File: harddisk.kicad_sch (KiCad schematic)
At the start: 12 parts, among them IC45 74HCT573, IC46 74HCT573, J1 IDC 44-pin IDE

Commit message: fix 44-pin ide
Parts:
- J1: footprint Connector_IDC:IDC-Header_2x22_P2.54mm_Vertical -> Connector_PinHeader_2.00mm:PinHeader_2x22_P2.00mm_Vertical
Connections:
- no-connect marks 6 -> 7
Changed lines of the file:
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@@
 	)
 	(no_connect
+		(at 74.93 66.04)
+	)
+	(no_connect
 		(at 74.93 60.96)
 	)
@@
 			)
 		)
-		(property "Footprint" "Connector_IDC:IDC-Header_2x22_P2.54mm_Vertical"
+		(property "Footprint" "Connector_PinHeader_2.00mm:PinHeader_2x22_P2.00mm_Vertical"
 			(at 80.01 53.34 0)
 			(effects

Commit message: prepare for fabrication
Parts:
- C217: LCSC (none) -> C344201; LCSC Part (none) -> C344201
- C75, C97: LCSC (none) -> C49678; LCSC Part (none) -> C49678
- IC45, IC46: LCSC (none) -> C52145555; LCSC Part (none) -> C52145555
- R204: LCSC (none) -> C2907326; LCSC Part (none) -> C2907326
- R205: LCSC (none) -> C2907219; LCSC Part (none) -> C2907219
- R206: LCSC (none) -> C2933293; LCSC Part (none) -> C2933293
- RN1: value 68R -> 68Rx8; LCSC (none) -> C1739978; LCSC Part (none) -> C1739978
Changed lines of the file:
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@@
+			)
+		)
+		(property "LCSC" "C2907326"
+			(at 97.79 81.28 90)
+			(effects
+				(font
+					(size 1.27 1.27)
+				)
+				(hide yes)
+			)
+		)
+		(property "LCSC Part" "C2907326"
+			(at 97.79 81.28 90)
+			(effects
+				(font
+					(size 1.27 1.27)
+				)
+				(hide yes)
 			)
 		)
@@
 		(property "Description" "Resistor, small symbol"
 			(at 115.57 63.5 0)
+			(effects
+				(font
+					(size 1.27 1.27)
+				)
+				(hide yes)
+			)
+		)
+		(property "LCSC" "C2907219"
+			(at 115.57 63.5 90)
+			(effects
+				(font
+					(size 1.27 1.27)
+				)
+				(hide yes)
+			)
+		)
+		(property "LCSC Part" "C2907219"
+			(at 115.57 63.5 90)
 			(effects
 				(font
@@
 			)
 		)
+		(property "LCSC" "C52145555"
+			(at 140.97 111.76 0)
+			(effects
+				(font
+					(size 1.27 1.27)
+				)
+				(hide yes)
+			)
+		)
+		(property "LCSC Part" "C52145555"
+			(at 140.97 111.76 0)
+			(effects
+				(font
+					(size 1.27 1.27)
+				)
+				(hide yes)
+			)
+		)
 		(pin "3"
 		)
@@
 		(property "Description" "Unpolarized capacitor, small symbol"
 			(at 62.23 161.29 0)
+			(effects
+				(font
+					(size 1.27 1.27)
+				)
+				(hide yes)
+			)
+		)
+		(property "LCSC" "C49678"
+			(at 62.23 161.29 90)
+			(effects
+				(font
+					(size 1.27 1.27)
+				)
+				(hide yes)
+			)
+		)
+		(property "LCSC Part" "C49678"
+			(at 62.23 161.29 90)
 			(effects
 				(font
@@
 			)
 		)
+		(property "LCSC" "C344201"
+			(at 128.27 38.1 0)
+			(effects
+				(font
+					(size 1.27 1.27)
+				)
+				(hide yes)
+			)
+		)
+		(property "LCSC Part" "C344201"
+			(at 128.27 38.1 0)
+			(effects
+				(font
+					(size 1.27 1.27)
+				)
+				(hide yes)
+			)
+		)
 		(pin "1"
 		)
@@
 			)
 		)
+		(property "LCSC" "C49678"
+			(at 68.58 161.29 90)
+			(effects
+				(font
+					(size 1.27 1.27)
+				)
+				(hide yes)
+			)
+		)
+		(property "LCSC Part" "C49678"
+			(at 68.58 161.29 90)
+			(effects
+				(font
+					(size 1.27 1.27)
+				)
+				(hide yes)
+			)
+		)
 		(pin "2"
 		)
@@
 			)
 		)
+		(property "LCSC" "C2933293"
+			(at 116.84 81.28 90)
+			(effects
+				(font
+					(size 1.27 1.27)
+				)
+				(hide yes)
+			)
+		)
+		(property "LCSC Part" "C2933293"
+			(at 116.84 81.28 90)
+			(effects
+				(font
+					(size 1.27 1.27)
+				)
+				(hide yes)
+			)
+		)
 		(pin "1"
 		)
@@
 			)
 		)
-		(property "Value" "68R"
+		(property "Value" "68Rx8"
 			(at 121.92 175.26 90)
 			(effects
@@
 		(property "Description" "8 resistor network, parallel topology"
 			(at 121.92 161.29 0)
+			(effects
+				(font
+					(size 1.27 1.27)
+				)
+				(hide yes)
+			)
+		)
+		(property "LCSC" "C1739978"
+			(at 121.92 161.29 90)
+			(effects
+				(font
+					(size 1.27 1.27)
+				)
+				(hide yes)
+			)
+		)
+		(property "LCSC Part" "C1739978"
+			(at 121.92 161.29 90)
 			(effects
 				(font
@@
 			(at 140.97 166.37 0)
 			(effects
+				(font
+					(size 1.27 1.27)
+				)
+				(hide yes)
+			)
+		)
+		(property "LCSC" "C52145555"
+			(at 140.97 166.37 0)
+			(effects
+				(font
+					(size 1.27 1.27)
+				)
+				(hide yes)
+			)
+		)
+		(property "LCSC Part" "C52145555"
+			(at 140.97 166.37 0)
+			(effects

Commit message: fix ide tristate buffer part selection
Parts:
- IC46: value 74HCT573 -> 74HC573; LCSC C52145555 -> C55388; LCSC Part C52145555 -> C55388
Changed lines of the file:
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@@
 			)
 		)
-		(property "Value" "74HCT573"
+		(property "Value" "74HC573"
 			(at 137.8519 93.98 0)
 			(effects
@@
 			)
 		)
-		(property "LCSC" "C52145555"
+		(property "LCSC" "C55388"
 			(at 140.97 111.76 0)
 			(effects
@@
 			)
 		)
-		(property "LCSC Part" "C52145555"
+		(property "LCSC Part" "C55388"
 			(at 140.97 111.76 0)
 			(effects

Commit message: fix missing ide signals
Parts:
- added R207: 10K, Resistor_SMD:R_0805_2012Metric, symbol Device:R_Small
- added U11: 74LVC1G04, Package_TO_SOT_SMD:SOT-353_SC-70-5, symbol 74xGxx:74LVC1G04
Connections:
- net +5V: now also U11.3 (GND)
- net GND: now also R207.1, U11.5 (VCC)
- net at J1.31 (Pin_31): now also R207.2, U11.2
- net Ior* renamed ~{Ior}
- net Iow* renamed ~{Iow}
- new net ~{I13}: U11.4
- no-connect marks 7 -> 6

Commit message: fix routing for ide and ram
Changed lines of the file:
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@@
 		)
 	)
-	(hierarchical_label "LA[2..21]"
+	(hierarchical_label "La[2..21]"
 		(shape input)
 		(at 60.96 92.71 180)

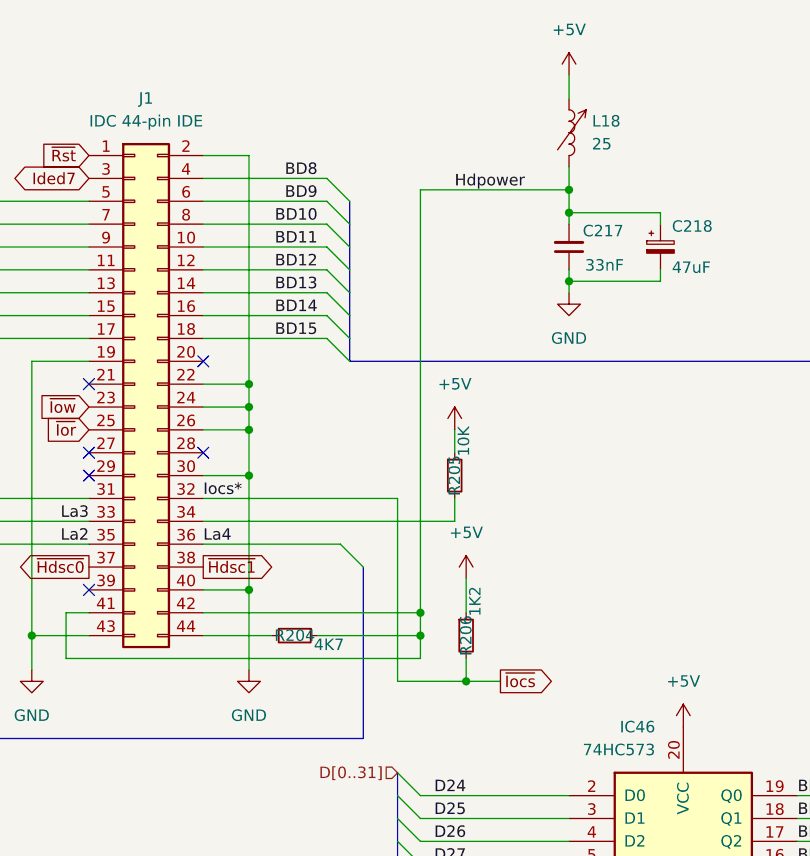
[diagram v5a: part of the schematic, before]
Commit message: fix power domains
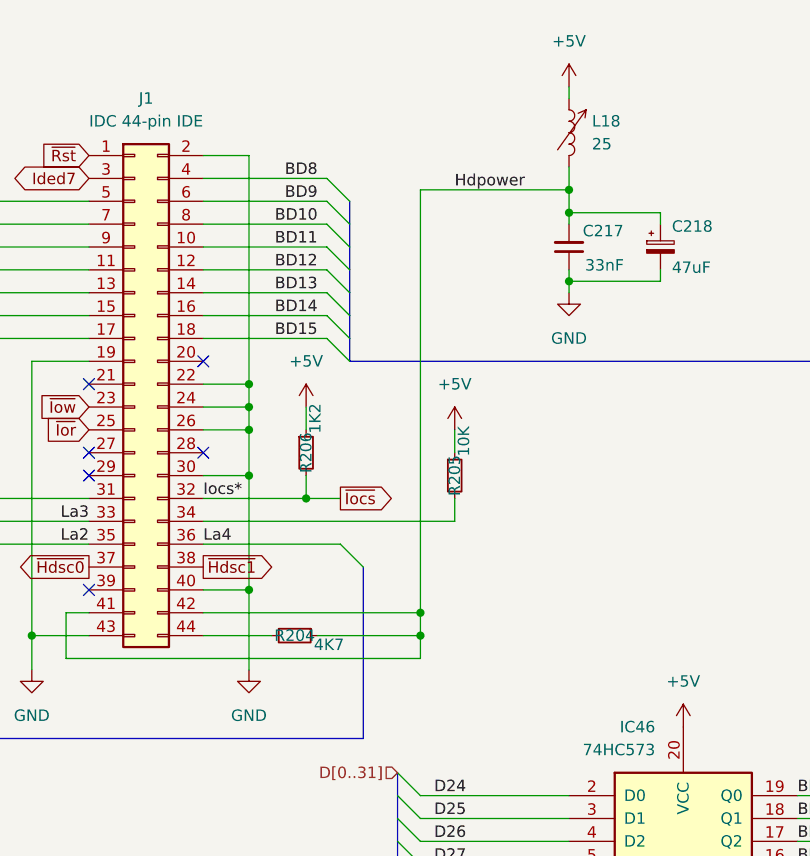
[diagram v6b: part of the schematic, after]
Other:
- moved on the sheet: R206
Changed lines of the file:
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@@
 	)
 	(junction
-		(at 116.84 86.36)
-		(diameter 0)
-		(color 0 0 0 0)
-	)
-	(junction
 		(at 92.71 55.88)
 		(diameter 0)
@@
 	)
 	(junction
+		(at 99.06 66.04)
+		(diameter 0)
+		(color 0 0 0 0)
+	)
+	(junction
 		(at 68.58 81.28)
 		(diameter 0)
@@
 	(wire
 		(pts
-			(xy 116.84 74.93) (xy 116.84 78.74)
+			(xy 99.06 55.88) (xy 99.06 58.42)
 		)
 		(stroke
@@
 	(wire
 		(pts
-			(xy 87.63 66.04) (xy 109.22 66.04)
+			(xy 87.63 66.04) (xy 99.06 66.04)
 		)
 		(stroke
@@
 	(wire
 		(pts
-			(xy 109.22 66.04) (xy 109.22 86.36)
-		)
-		(stroke
-			(width 0)
-			(type default)
-		)
-	)
-	(wire
-		(pts
 			(xy 92.71 76.2) (xy 92.71 85.09)
 		)
@@
 	(wire
 		(pts
-			(xy 116.84 83.82) (xy 116.84 86.36)
+			(xy 99.06 63.5) (xy 99.06 66.04)
 		)
 		(stroke
@@
 	(wire
 		(pts
-			(xy 109.22 86.36) (xy 116.84 86.36)
-		)
-		(stroke
-			(width 0)
-			(type default)
-		)
-	)
-	(wire
-		(pts
 			(xy 127 163.83) (xy 128.27 163.83)
 		)
@@
 	(wire
 		(pts
-			(xy 128.27 19.05) (xy 128.27 21.59)
+			(xy 128.27 20.32) (xy 128.27 21.59)
 		)
 		(stroke
@@
 	(wire
 		(pts
-			(xy 116.84 86.36) (xy 120.65 86.36)
+			(xy 153.67 109.22) (xy 161.29 109.22)
 		)
 		(stroke
@@
 	(wire
 		(pts
-			(xy 153.67 109.22) (xy 161.29 109.22)
+			(xy 153.67 166.37) (xy 161.29 166.37)
 		)
 		(stroke
@@
 		)
 	)
-	(wire
+	(bus
 		(pts
-			(xy 153.67 166.37) (xy 161.29 166.37)
+			(xy 60.96 73.66) (xy 60.96 92.71)
 		)
 		(stroke
@@
 		)
 	)
-	(bus
+	(wire
 		(pts
-			(xy 60.96 73.66) (xy 60.96 92.71)
+			(xy 127 153.67) (xy 128.27 153.67)
 		)
 		(stroke
@@
 	(wire
 		(pts
-			(xy 127 153.67) (xy 128.27 153.67)
+			(xy 99.06 66.04) (xy 102.87 66.04)
 		)
 		(stroke
@@
 	(global_label "~{Iocs}"
 		(shape output)
-		(at 120.65 86.36 0)
+		(at 102.87 66.04 0)
 		(fields_autoplaced yes)
 		(effects
@@
 		)
 		(property "Intersheetrefs" "${INTERSHEET_REFS}"
-			(at 127.5057 86.36 0)
+			(at 109.7257 66.04 0)
 			(effects
 				(font
@@
 	(symbol
 		(lib_id "power:+5V")
-		(at 116.84 74.93 0)
+		(at 99.06 55.88 0)
 		(mirror y)
 		(unit 1)
@@
 		(fields_autoplaced yes)
 		(property "Reference" "#PWR0320"
-			(at 116.84 78.74 0)
+			(at 99.06 59.69 0)
 			(effects
 				(font
@@
 		)
 		(property "Value" "+5V"
-			(at 116.84 69.85 0)
+			(at 99.06 50.8 0)
 			(effects
 				(font
@@
 		)
 		(property "Footprint" ""
-			(at 116.84 74.93 0)
+			(at 99.06 55.88 0)
 			(effects
 				(font
@@
 		)
 		(property "Datasheet" ""
-			(at 116.84 74.93 0)
+			(at 99.06 55.88 0)
 			(effects
 				(font
@@
 		)
 		(property "Description" "Power symbol creates a global label with name \"+5V\""
-			(at 116.84 74.93 0)
+			(at 99.06 55.88 0)
 			(effects
 				(font
@@
 	(symbol
 		(lib_id "power:+5V")
-		(at 128.27 19.05 0)
+		(at 128.27 20.32 0)
 		(mirror y)
 		(unit 1)
@@
 		(fields_autoplaced yes)
 		(property "Reference" "#PWR0322"
-			(at 128.27 22.86 0)
+			(at 128.27 24.13 0)
 			(effects
 				(font
@@
 		)
 		(property "Value" "+5V"
-			(at 128.27 13.97 0)
+			(at 128.27 15.24 0)
 			(effects
 				(font
@@
 		)
 		(property "Footprint" ""
-			(at 128.27 19.05 0)
+			(at 128.27 20.32 0)
 			(effects
 				(font
@@
 		)
 		(property "Datasheet" ""
-			(at 128.27 19.05 0)
+			(at 128.27 20.32 0)
 			(effects
 				(font
@@
 		)
 		(property "Description" "Power symbol creates a global label with name \"+5V\""
-			(at 128.27 19.05 0)
+			(at 128.27 20.32 0)
 			(effects
 				(font
@@
 	(symbol
 		(lib_id "Device:R_Small")
-		(at 116.84 81.28 0)
+		(at 99.06 60.96 0)
 		(unit 1)
 		(exclude_from_sim no)
@@
 		(dnp no)
 		(property "Reference" "R206"
-			(at 116.84 81.28 90)
+			(at 99.06 60.96 90)
 			(effects
 				(font
@@
 		)
 		(property "Value" "1K2"
-			(at 117.856 77.47 90)
+			(at 100.076 57.15 90)
 			(effects
 				(font
@@
 		)
 		(property "Footprint" "Resistor_SMD:R_0805_2012Metric"
-			(at 116.84 81.28 0)
+			(at 99.06 60.96 0)
 			(effects
 				(font
@@
 		)
 		(property "Datasheet" "~"
-			(at 116.84 81.28 0)
+			(at 99.06 60.96 0)
 			(effects
 				(font
@@
 		)
 		(property "Description" "Resistor, small symbol"
-			(at 116.84 81.28 0)
+			(at 99.06 60.96 0)
 			(effects
 				(font
@@
 		)
 		(property "LCSC" "C2933293"
-			(at 116.84 81.28 90)
+			(at 99.06 60.96 90)
 			(effects
 				(font
@@
 		)
 		(property "LCSC Part" "C2933293"
-			(at 116.84 81.28 90)
+			(at 99.06 60.96 90)
 			(effects
 				(font

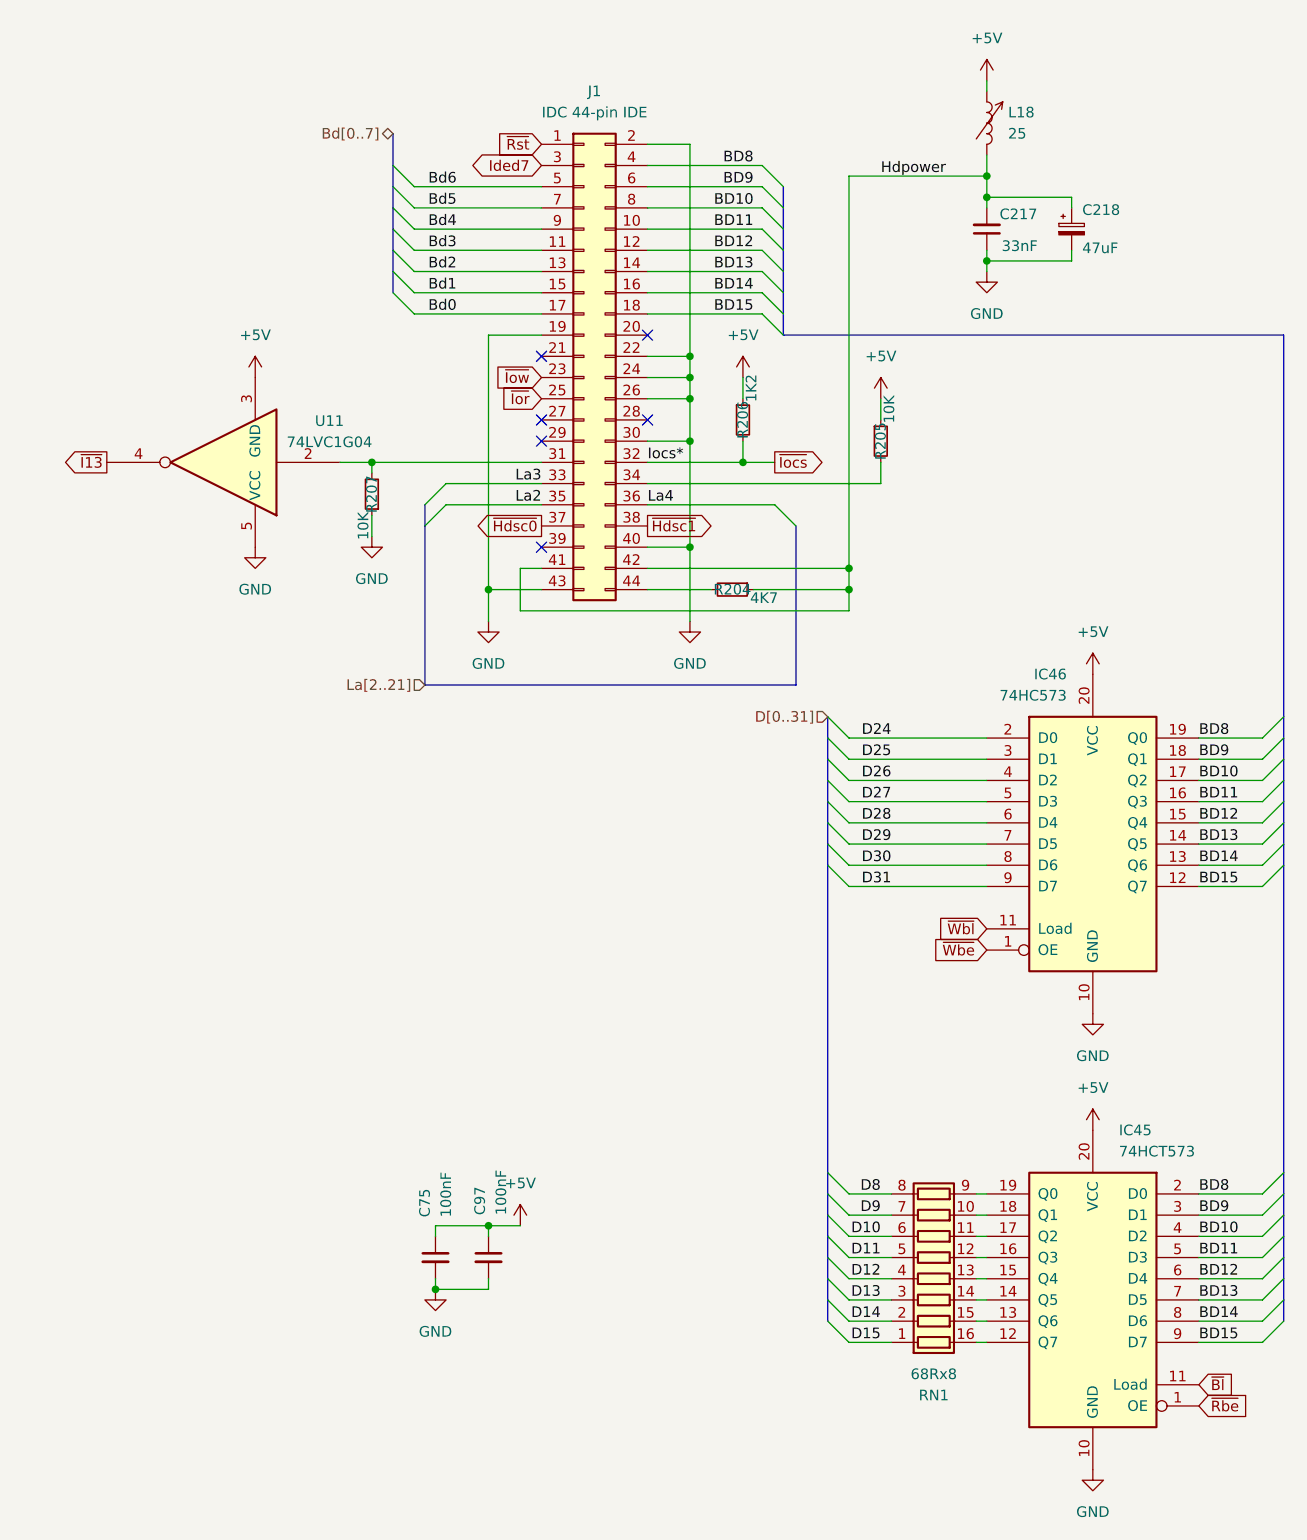
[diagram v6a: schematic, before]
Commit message: verify all component values vs TRM
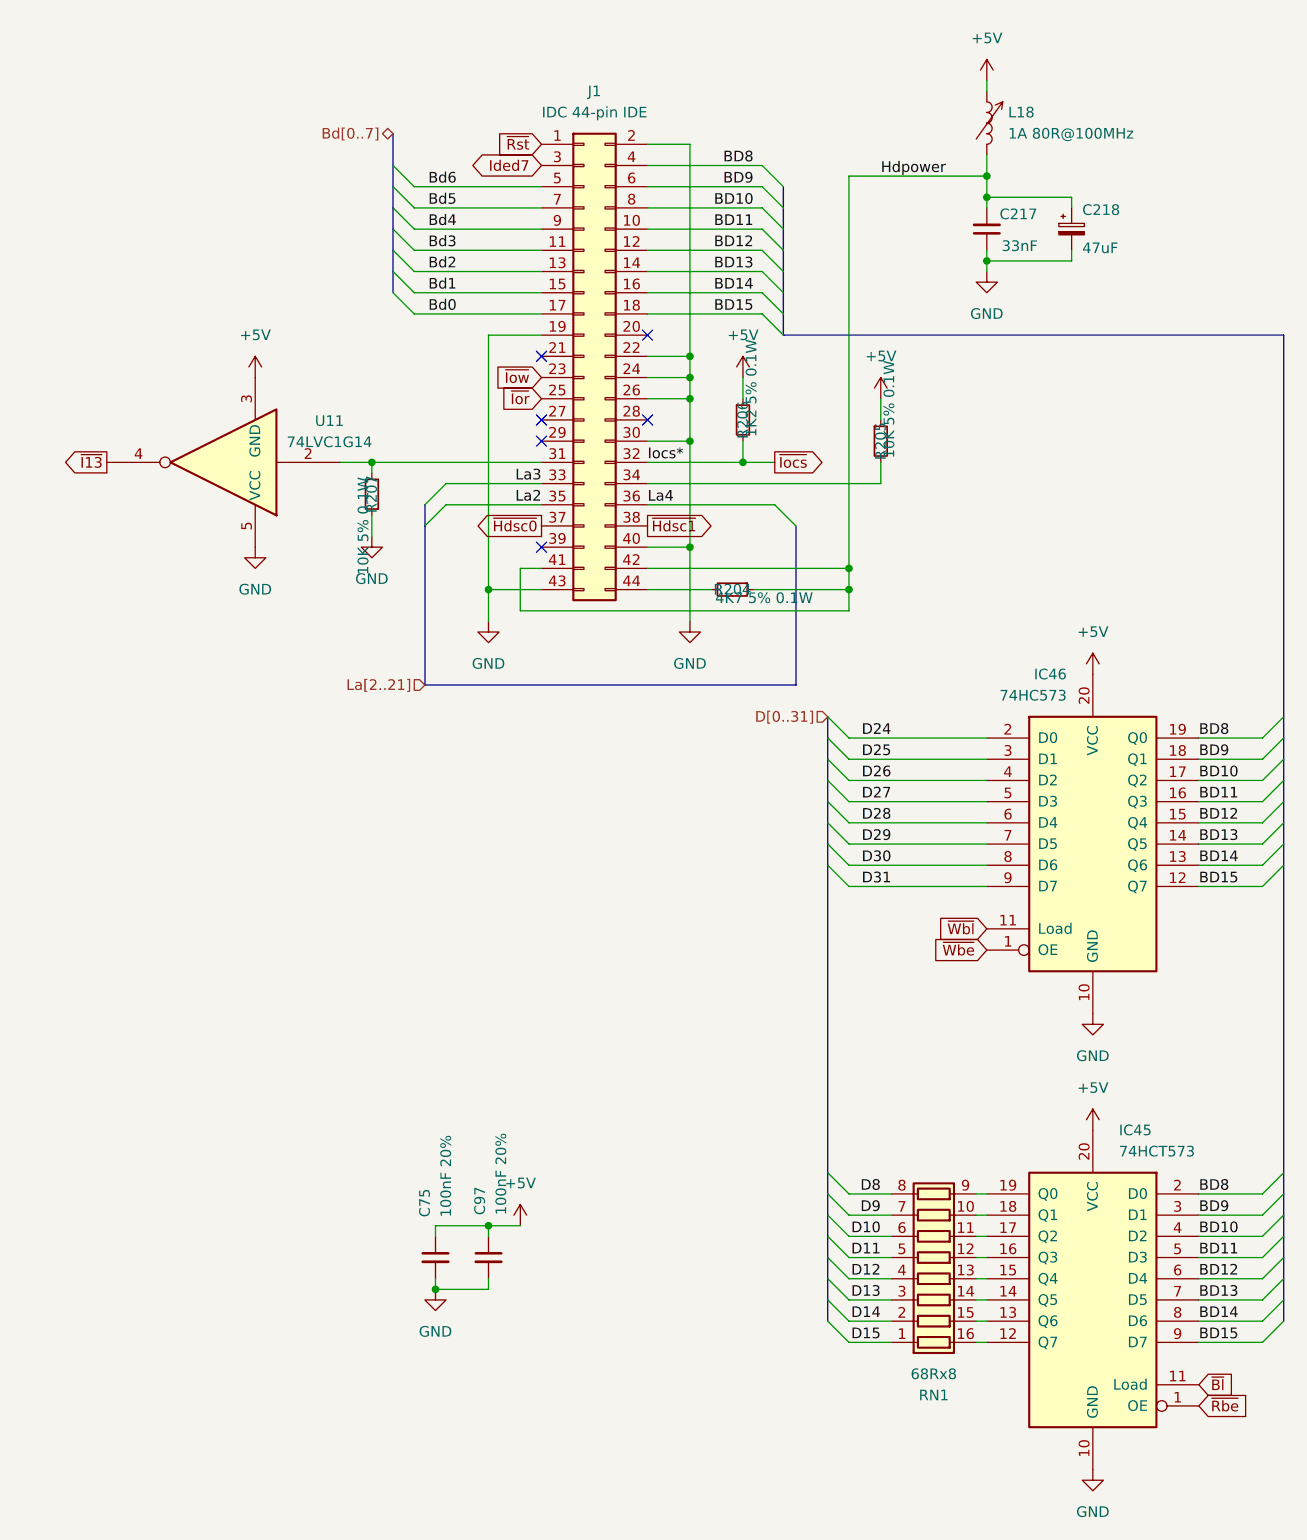
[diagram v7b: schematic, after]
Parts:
- C75, C97: value 100nF -> 100nF 20%
- L18: value 25 -> 1A 80R@100MHz
- R204: value 4K7 -> 4K7 5% 0.1W
- R205, R207: value 10K -> 10K 5% 0.1W
- R206: value 1K2 -> 1K2 5% 0.1W
- U11: value 74LVC1G04 -> 74LVC1G14
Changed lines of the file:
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@@
 			)
 		)
-		(property "Value" "4K7"
+		(property "Value" "4K7 5% 0.1W"
 			(at 101.6 82.296 90)
 			(effects
@@
 			)
 		)
-		(property "Value" "10K"
+		(property "Value" "10K 5% 0.1W"
 			(at 116.586 59.69 90)
 			(effects
@@
 			)
 		)
-		(property "Value" "74LVC1G04"
+		(property "Value" "74LVC1G14"
 			(at 49.53 63.6268 0)
 			(effects
@@
 			)
 		)
-		(property "Value" "100nF"
+		(property "Value" "100nF 20%"
 			(at 63.5 156.464 90)
 			(effects
@@
 			)
 		)
-		(property "Value" "100nF"
+		(property "Value" "100nF 20%"
 			(at 70.104 156.21 90)
 			(effects
@@
 			)
 		)
-		(property "Value" "1K2"
+		(property "Value" "1K2 5% 0.1W"
 			(at 100.076 57.15 90)
 			(effects
@@
 			)
 		)
-		(property "Value" "25"
+		(property "Value" "1A 80R@100MHz"
 			(at 130.81 26.6699 0)
 			(effects
@@
 			)
 		)
-		(property "Value" "10K"
+		(property "Value" "10K 5% 0.1W"
 			(at 53.594 73.66 90)
 			(effects
